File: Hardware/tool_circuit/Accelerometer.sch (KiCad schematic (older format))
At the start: 1 part, among them J2 Conn_01x08_Female

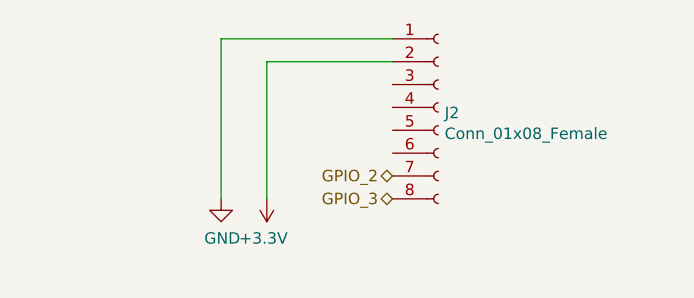
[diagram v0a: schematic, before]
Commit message: Tool Circuit schematic updates
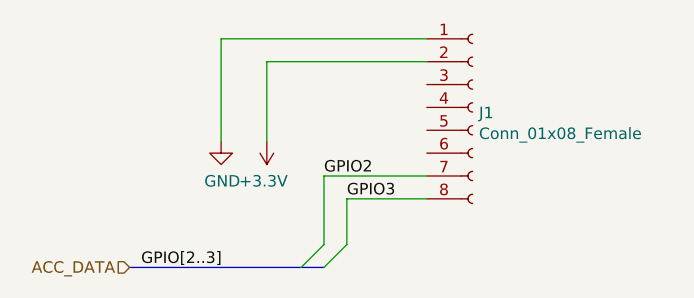
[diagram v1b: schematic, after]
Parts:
- renumbered J2 to J1
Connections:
- net GPIO_2 renamed GPIO2
- net GPIO_3 renamed GPIO3
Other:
- moved on the sheet: J1
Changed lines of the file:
@@
 $Descr A4 11693 8268
 encoding utf-8
-Sheet 7 7
+Sheet 6 8
 Title ""
 Date ""
@@
 Comment4 ""
 $EndDescr
+Wire Wire Line
+	5550 4200 5550 3900
+Wire Wire Line
+	5650 4200 5650 4000
+Text Label 5550 3900 0    50   ~ 0
+GPIO2
+Text Label 5650 4000 0    50   ~ 0
+GPIO3
+Text Label 4750 4300 0    50   ~ 0
+GPIO[2..3]
+Text HLabel 4700 4300 0    50   Input ~ 0
+ACC_DATA
+Entry Wire Line
+	5550 4300 5650 4200
+Entry Wire Line
+	5450 4300 5550 4200
 $Comp
-L Connector:Conn_01x08_Female J2
+L Connector:Conn_01x08_Female J1
 U 1 1 6149E3EA
-P 6050 3600
-F 0 "J2" H 6078 3576 50  0000 L CNN
-F 1 "Conn_01x08_Female" H 6078 3485 50  0000 L CNN
-F 2 "Connector_PinHeader_2.54mm:PinHeader_1x08_P2.54mm_Vertical" H 6050 3600 50  0001 C CNN
-F 3 "~" H 6050 3600 50  0001 C CNN
-	1    6050 3600
-	1    0    0    -1
-$EndComp
-$Comp
-L power:GND #PWR0108
-U 1 1 6149F537
-P 5100 4000
-F 0 "#PWR0108" H 5100 3750 50  0001 C CNN
-F 1 "GND" H 5105 3827 50  0000 C CNN
-F 2 "" H 5100 4000 50  0001 C CNN
-F 3 "" H 5100 4000 50  0001 C CNN
-	1    5100 4000
+P 6200 3600
+F 0 "J1" H 6228 3576 50  0000 L CNN
+F 1 "Conn_01x08_Female" H 6228 3485 50  0000 L CNN
+F 2 "Connector_PinHeader_2.54mm:PinHeader_1x08_P2.54mm_Vertical" H 6200 3600 50  0001 C CNN
+F 3 "~" H 6200 3600 50  0001 C CNN
+	1    6200 3600
 	1    0    0    -1
 $EndComp
 Wire Wire Line
-	5850 3300 5100 3300
+	5650 4000 6000 4000
 Wire Wire Line
-	5100 3300 5100 4000
+	5550 3900 6000 3900
+Wire Wire Line
+	5300 3400 6000 3400
+Wire Wire Line
+	5100 3300 6000 3300
 $Comp
-L power:+3.3V #PWR0109
+L power:+3.3V #PWR07
 U 1 1 614A0E05
-P 5300 4000
-F 0 "#PWR0109" H 5300 3850 50  0001 C CNN
-F 1 "+3.3V" H 5315 4173 50  0000 C CNN
-F 2 "" H 5300 4000 50  0001 C CNN
-F 3 "" H 5300 4000 50  0001 C CNN
-	1    5300 4000
+P 5300 3750
+F 0 "#PWR07" H 5300 3600 50  0001 C CNN
+F 1 "+3.3V" H 5315 3923 50  0000 C CNN
+F 2 "" H 5300 3750 50  0001 C CNN
+F 3 "" H 5300 3750 50  0001 C CNN
+	1    5300 3750
 	-1   0    0    1
 $EndComp
+$Comp
+L power:GND #PWR06
+U 1 1 6149F537
+P 5100 3750
+F 0 "#PWR06" H 5100 3500 50  0001 C CNN
+F 1 "GND" H 5105 3577 50  0000 C CNN
+F 2 "" H 5100 3750 50  0001 C CNN
+F 3 "" H 5100 3750 50  0001 C CNN
+	1    5100 3750
+	1    0    0    -1
+$EndComp
 Wire Wire Line
-	5850 3400 5300 3400
+	5100 3300 5100 3750
 Wire Wire Line
-	5300 3400 5300 4000
-Text HLabel 5850 3900 0    50   BiDi ~ 0
-GPIO_2
-Text HLabel 5850 4000 0    50   BiDi ~ 0
-GPIO_3
+	5300 3400 5300 3750
+Wire Bus Line
+	4700 4300 5550 4300
 $EndSCHEMATC

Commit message: schematic revisions
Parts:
- renumbered J1 to J3
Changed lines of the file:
@@
 $Descr A4 11693 8268
 encoding utf-8
-Sheet 6 8
+Sheet 7 8
 Title ""
 Date ""
@@
 	5450 4300 5550 4200
 $Comp
-L Connector:Conn_01x08_Female J1
+L Connector:Conn_01x08_Female J3
 U 1 1 6149E3EA
 P 6200 3600
-F 0 "J1" H 6228 3576 50  0000 L CNN
+F 0 "J3" H 6228 3576 50  0000 L CNN
 F 1 "Conn_01x08_Female" H 6228 3485 50  0000 L CNN
 F 2 "Connector_PinHeader_2.54mm:PinHeader_1x08_P2.54mm_Vertical" H 6200 3600 50  0001 C CNN
@@
 	5100 3300 6000 3300
 $Comp
-L power:+3.3V #PWR07
+L power:+3.3V #PWR011
 U 1 1 614A0E05
 P 5300 3750
-F 0 "#PWR07" H 5300 3600 50  0001 C CNN
+F 0 "#PWR011" H 5300 3600 50  0001 C CNN
 F 1 "+3.3V" H 5315 3923 50  0000 C CNN
 F 2 "" H 5300 3750 50  0001 C CNN
@@
 $EndComp
 $Comp
-L power:GND #PWR06
+L power:GND #PWR010
 U 1 1 6149F537
 P 5100 3750
-F 0 "#PWR06" H 5100 3500 50  0001 C CNN
+F 0 "#PWR010" H 5100 3500 50  0001 C CNN
 F 1 "GND" H 5105 3577 50  0000 C CNN
 F 2 "" H 5100 3750 50  0001 C CNN

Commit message: made some post review changes
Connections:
- no-connect marks 0 -> 4
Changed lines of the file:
@@
 Text Label 5650 4000 0    50   ~ 0
 GPIO3
-Text Label 4750 4300 0    50   ~ 0
-GPIO[2..3]
-Text HLabel 4700 4300 0    50   Input ~ 0
+Text HLabel 4700 4300 0    50   BiDi ~ 0
 ACC_DATA
 Entry Wire Line
@@
 Wire Wire Line
 	5300 3400 5300 3750
+NoConn ~ 6000 3500
+NoConn ~ 6000 3600
+NoConn ~ 6000 3700
+NoConn ~ 6000 3800
 Wire Bus Line
 	4700 4300 5550 4300

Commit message: layout
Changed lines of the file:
@@
 Wire Wire Line
 	5300 3400 6000 3400
-Wire Wire Line
-	5100 3300 6000 3300
 $Comp
-L power:+3.3V #PWR012
+L power:+3.3V #PWR010
 U 1 1 614A0E05
 P 5300 3750
-F 0 "#PWR012" H 5300 3600 50  0001 C CNN
+F 0 "#PWR010" H 5300 3600 50  0001 C CNN
 F 1 "+3.3V" H 5315 3923 50  0000 C CNN
 F 2 "" H 5300 3750 50  0001 C CNN
@@
 	-1   0    0    1
 $EndComp
-$Comp
-L power:GND #PWR011
-U 1 1 6149F537
-P 5100 3750
-F 0 "#PWR011" H 5100 3500 50  0001 C CNN
-F 1 "GND" H 5105 3577 50  0000 C CNN
-F 2 "" H 5100 3750 50  0001 C CNN
-F 3 "" H 5100 3750 50  0001 C CNN
-	1    5100 3750
-	1    0    0    -1
-$EndComp
-Wire Wire Line
-	5100 3300 5100 3750
 Wire Wire Line
 	5300 3400 5300 3750
@@
 Wire Bus Line
 	4700 4300 5550 4300
+$Comp
+L power:GND #PWR011
+U 1 1 617F6689
+P 6000 3300
+F 0 "#PWR011" H 6000 3050 50  0001 C CNN
+F 1 "GND" V 6005 3172 50  0000 R CNN
+F 2 "" H 6000 3300 50  0001 C CNN
+F 3 "" H 6000 3300 50  0001 C CNN
+	1    6000 3300
+	0    1    1    0
+$EndComp
 $EndSCHEMATC

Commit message: pcb revisions
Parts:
- J3: value Conn_01x08_Female -> Accel.
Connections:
- net GPIO2 renamed GPIO2_SDA1
- net GPIO3 renamed GPIO3_SCL1
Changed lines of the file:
@@
 $Descr A4 11693 8268
 encoding utf-8
-Sheet 7 8
+Sheet 8 8
 Title "Accelerometer "
 Date ""
@@
 Comment4 ""
 $EndDescr
-Wire Wire Line
-	5550 4200 5550 3900
-Wire Wire Line
-	5650 4200 5650 4000
-Text Label 5550 3900 0    50   ~ 0
-GPIO2
-Text Label 5650 4000 0    50   ~ 0
-GPIO3
-Text HLabel 4700 4300 0    50   BiDi ~ 0
-ACC_DATA
-Entry Wire Line
-	5550 4300 5650 4200
-Entry Wire Line
-	5450 4300 5550 4200
 $Comp
 L Connector:Conn_01x08_Female J3
@@
 P 6200 3600
 F 0 "J3" H 6228 3576 50  0000 L CNN
-F 1 "Conn_01x08_Female" H 6228 3485 50  0000 L CNN
+F 1 "Accel." H 6228 3485 50  0000 L CNN
 F 2 "Connector_PinHeader_2.54mm:PinHeader_1x08_P2.54mm_Vertical" H 6200 3600 50  0001 C CNN
 F 3 "~" H 6200 3600 50  0001 C CNN
@@
 	1    0    0    -1
 $EndComp
-Wire Wire Line
-	5650 4000 6000 4000
 Wire Wire Line
 	5300 3400 6000 3400
@@
 NoConn ~ 6000 3700
 NoConn ~ 6000 3800
-Wire Wire Line
-	5550 3900 6000 3900
 $Comp
 L power:GND #PWR011
@@
 	0    1    1    0
 $EndComp
-Wire Bus Line
-	4700 4300 5550 4300
+Text GLabel 6000 3900 0    50   BiDi ~ 0
+GPIO2_SDA1
+Text GLabel 6000 4000 0    50   BiDi ~ 0
+GPIO3_SCL1
 $EndSCHEMATC
